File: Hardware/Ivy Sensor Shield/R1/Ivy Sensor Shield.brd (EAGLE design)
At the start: 50.8 x 41.3 mm, 28 parts, among them IC2 MCP73831/OT

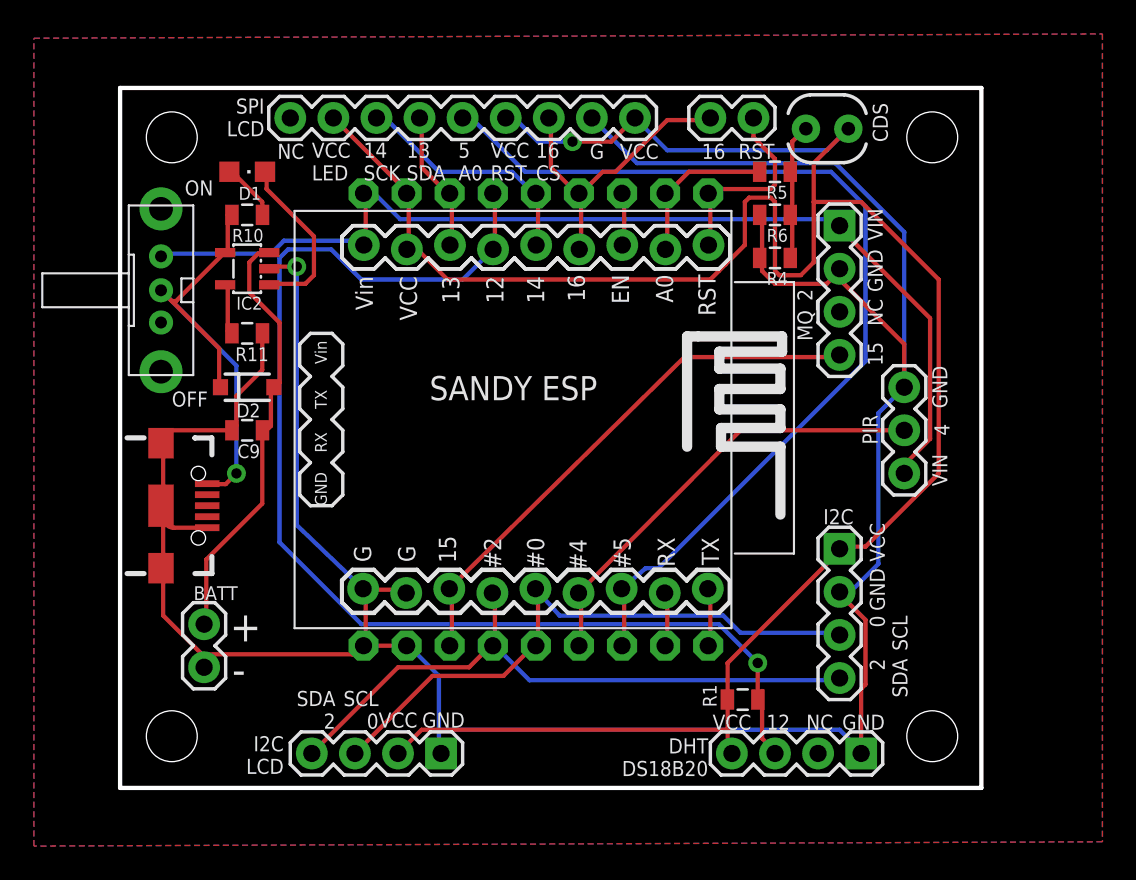
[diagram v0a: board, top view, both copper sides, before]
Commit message: Update Ivy Sensor to use Wemos D1 Mini
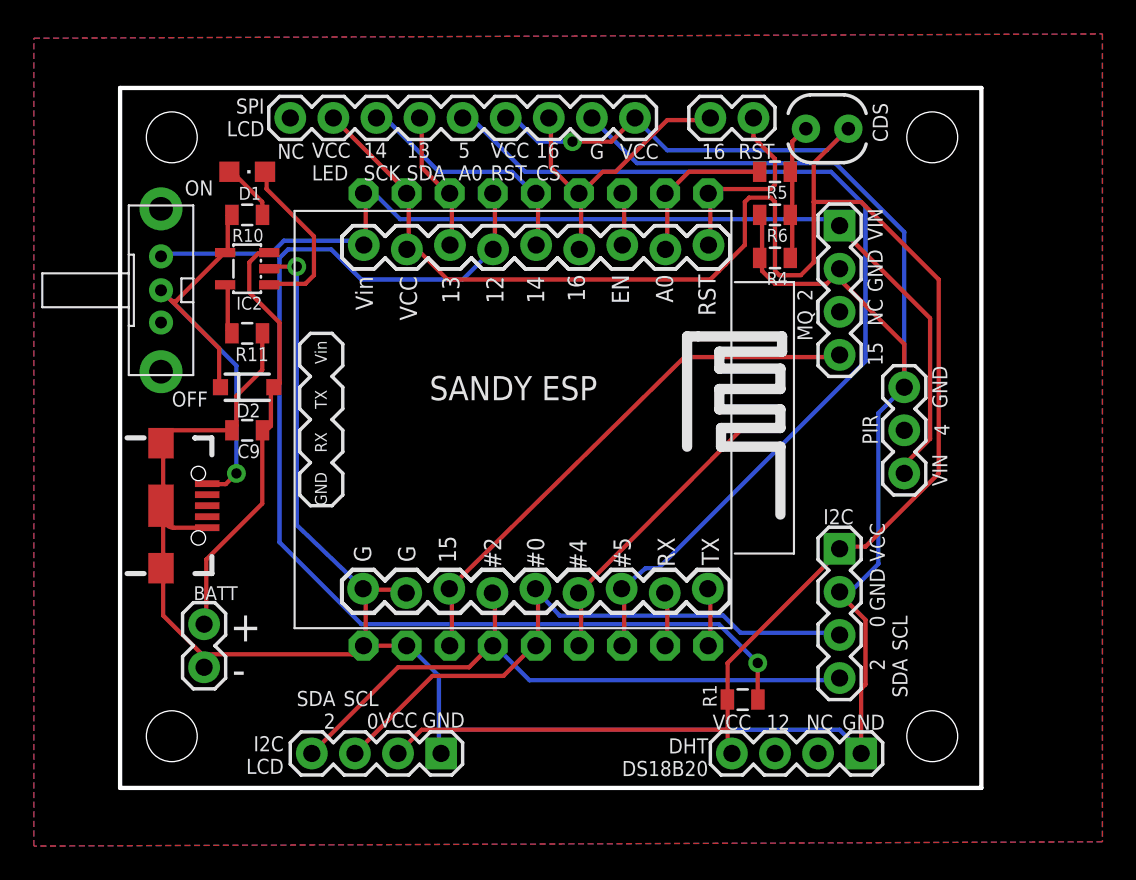
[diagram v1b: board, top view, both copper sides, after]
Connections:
- net 12: no longer DHT_DS18B20.3, R1.1
- net 15: now also SPI_TFT.5
- net 4: now also DHT_DS18B20.3, R1.1; no longer PIR.2
- net 5: now also PIR.2; no longer SPI_TFT.5
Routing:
- net 4: track 26.5 -> 16.9 mm
- net 12: track 72.3 -> 67.7 mm
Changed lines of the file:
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@@
 <contactref element="U$2" pad="5"/>
 <contactref element="JP3" pad="3"/>
-<contactref element="SPI_TFT" pad="5"/>
 <wire x1="55.88" y1="48.768" x2="55.88" y2="45.72" width="0.254" layer="1"/>
 <wire x1="55.88" y1="45.72" x2="55.753" y2="45.72" width="0.254" layer="1"/>
@@
 <wire x1="57.15" y1="50.292" x2="57.912" y2="50.292" width="0.254" layer="16"/>
 <wire x1="55.729" y1="49.082" x2="57.15" y2="50.292" width="0.254" layer="16"/>
-<wire x1="46.482" y1="76.708" x2="46.355" y2="76.835" width="0.254" layer="16"/>
+<contactref element="PIR" pad="2"/>
+<wire x1="70.104" y1="62.484" x2="72.39" y2="58.42" width="0" layer="19" extent="16-16"/>
 </signal>
 <signal name="4">
 <contactref element="U$2" pad="4"/>
 <contactref element="JP3" pad="4"/>
-<contactref element="PIR" pad="2"/>
 <wire x1="53.34" y1="48.768" x2="53.34" y2="45.72" width="0.254" layer="1"/>
 <wire x1="53.34" y1="45.72" x2="53.213" y2="45.72" width="0.254" layer="1"/>
 <wire x1="53.34" y1="48.768" x2="53.189" y2="48.828" width="0.254" layer="1"/>
-<wire x1="62.738" y1="58.42" x2="72.39" y2="58.42" width="0.254" layer="1"/>
 <wire x1="53.189" y1="48.828" x2="62.738" y2="58.42" width="0.254" layer="1"/>
+<contactref element="R1" pad="1"/>
+<contactref element="DHT_DS18B20" pad="3"/>
+<wire x1="64.77" y1="39.37" x2="63.765" y2="42.545" width="0" layer="19" extent="1-1"/>
+<wire x1="53.34" y1="45.72" x2="63.765" y2="42.545" width="0" layer="19" extent="1-1"/>
 </signal>
 <signal name="14">
@@
 <contactref element="JP1" pad="4"/>
 <contactref element="U$2" pad="12"/>
-<contactref element="DHT_DS18B20" pad="3"/>
-<contactref element="R1" pad="1"/>
-<wire x1="64.008" y1="40.259" x2="64.008" y2="43.053" width="0.254" layer="1"/>
-<wire x1="64.77" y1="39.497" x2="64.008" y2="40.259" width="0.254" layer="1"/>
-<wire x1="64.008" y1="43.053" x2="63.765" y2="42.545" width="0.254" layer="1"/>
-<wire x1="64.77" y1="39.497" x2="64.77" y2="39.37" width="0.254" layer="1"/>
 <wire x1="48.26" y1="69.342" x2="48.26" y2="72.39" width="0.254" layer="1"/>
 <wire x1="48.26" y1="72.39" x2="48.133" y2="72.39" width="0.254" layer="1"/>
@@
 <wire x1="38.608" y1="69.088" x2="36.068" y2="69.088" width="0.254" layer="16"/>
 <wire x1="40.386" y1="67.31" x2="38.608" y2="69.088" width="0.254" layer="16"/>
-<wire x1="63.754" y1="42.672" x2="63.765" y2="42.545" width="0.254" layer="1"/>
 <via x="63.754" y="44.704" extent="1-16" drill="0.6096"/>
 <wire x1="40.386" y1="67.31" x2="46.371" y2="67.31" width="0.254" layer="16"/>
@@
 <wire x1="45.569" y1="49.082" x2="59.436" y2="62.738" width="0.254" layer="1"/>
 <wire x1="68.58" y1="62.738" x2="68.58" y2="62.865" width="0.254" layer="1"/>
+<contactref element="SPI_TFT" pad="5"/>
+<wire x1="59.436" y1="62.738" x2="46.355" y2="76.835" width="0" layer="19" extent="1-1"/>
 </signal>
 <signal name="AOUT">
